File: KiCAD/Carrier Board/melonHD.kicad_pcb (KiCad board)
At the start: 4 copper layers, 39 x 20 mm, 16 parts, among them J1 XUNPU TYPEC-324G-BCP24 or GCT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, J2 XUNPU HDMI-201 or Würth 68511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, U2 ESD204DQAR-ES, U3 ESD204DQAR-ES, U4 ESD204DQAR-ES

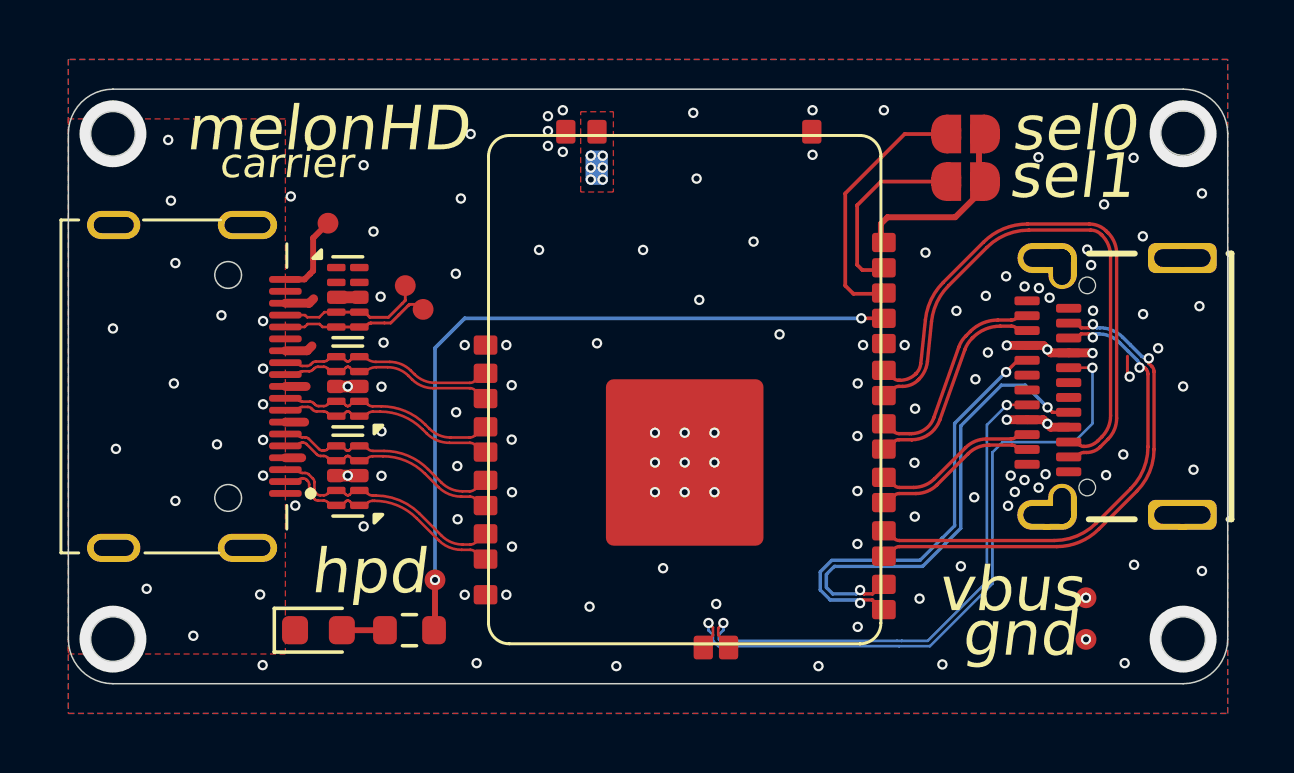
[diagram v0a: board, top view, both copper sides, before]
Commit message: Update carrier board and fix 3D embed
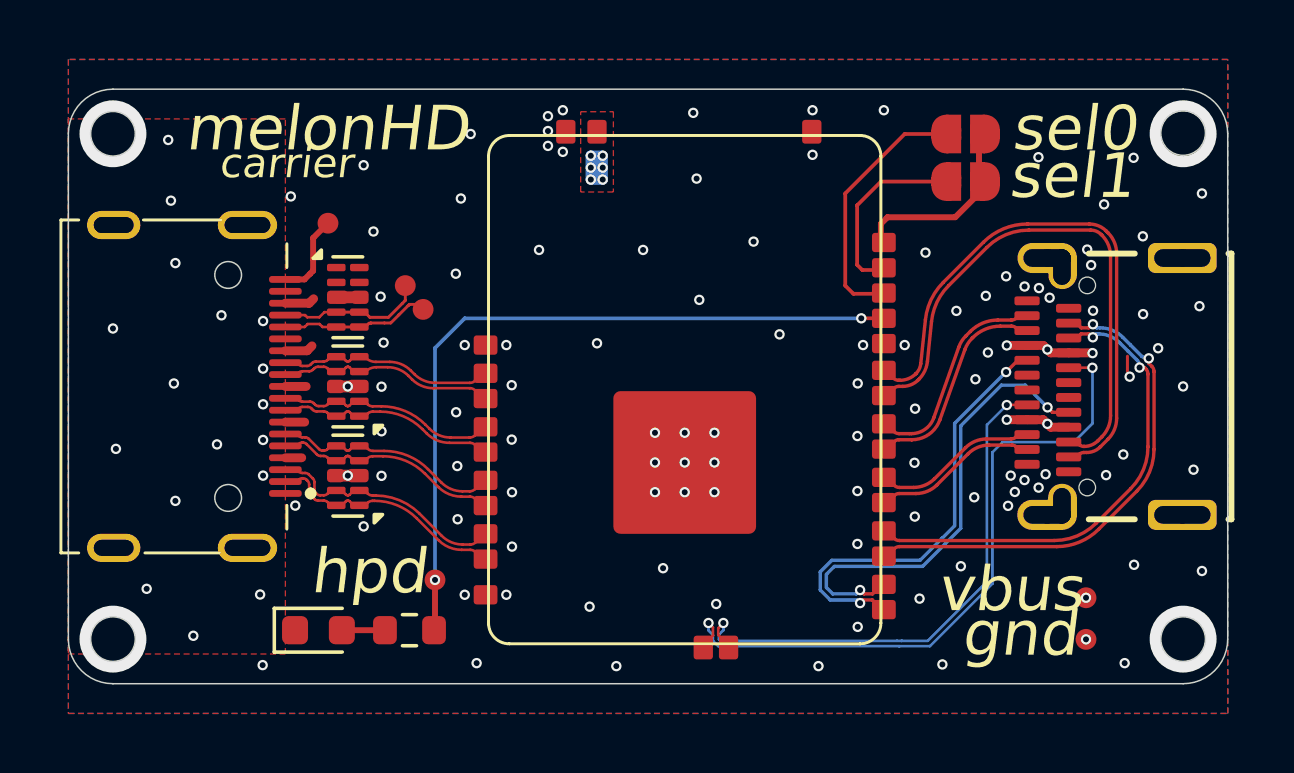
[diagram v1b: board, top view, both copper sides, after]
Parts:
- J1: value XUNPU TYPEC-324G-BCP24 or GCT USB4080-03-A -> GCT USB4080-03-A or XUNPU TYPEC-324G-BCP24
- U1: footprint melonHD:melonHD_SMT -> melonhd_module:melonHD_SMT
